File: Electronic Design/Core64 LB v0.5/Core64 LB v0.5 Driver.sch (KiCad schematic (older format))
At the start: 68 parts, among them J11 SSW-116-22-F-S-VS‎, J13 Core Cur. Mon., J14 SSW-116-22-F-S-VS‎, Q10 MMBT4403LT1G, Q11 MMBT4403LT1G, Q12 MMBT4401LT1G, Q13 MMBT4403LT1G, Q14 MMBT4403LT1G, Q15 MMBT4401LT1G, Q16 MMBT4403LT1G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

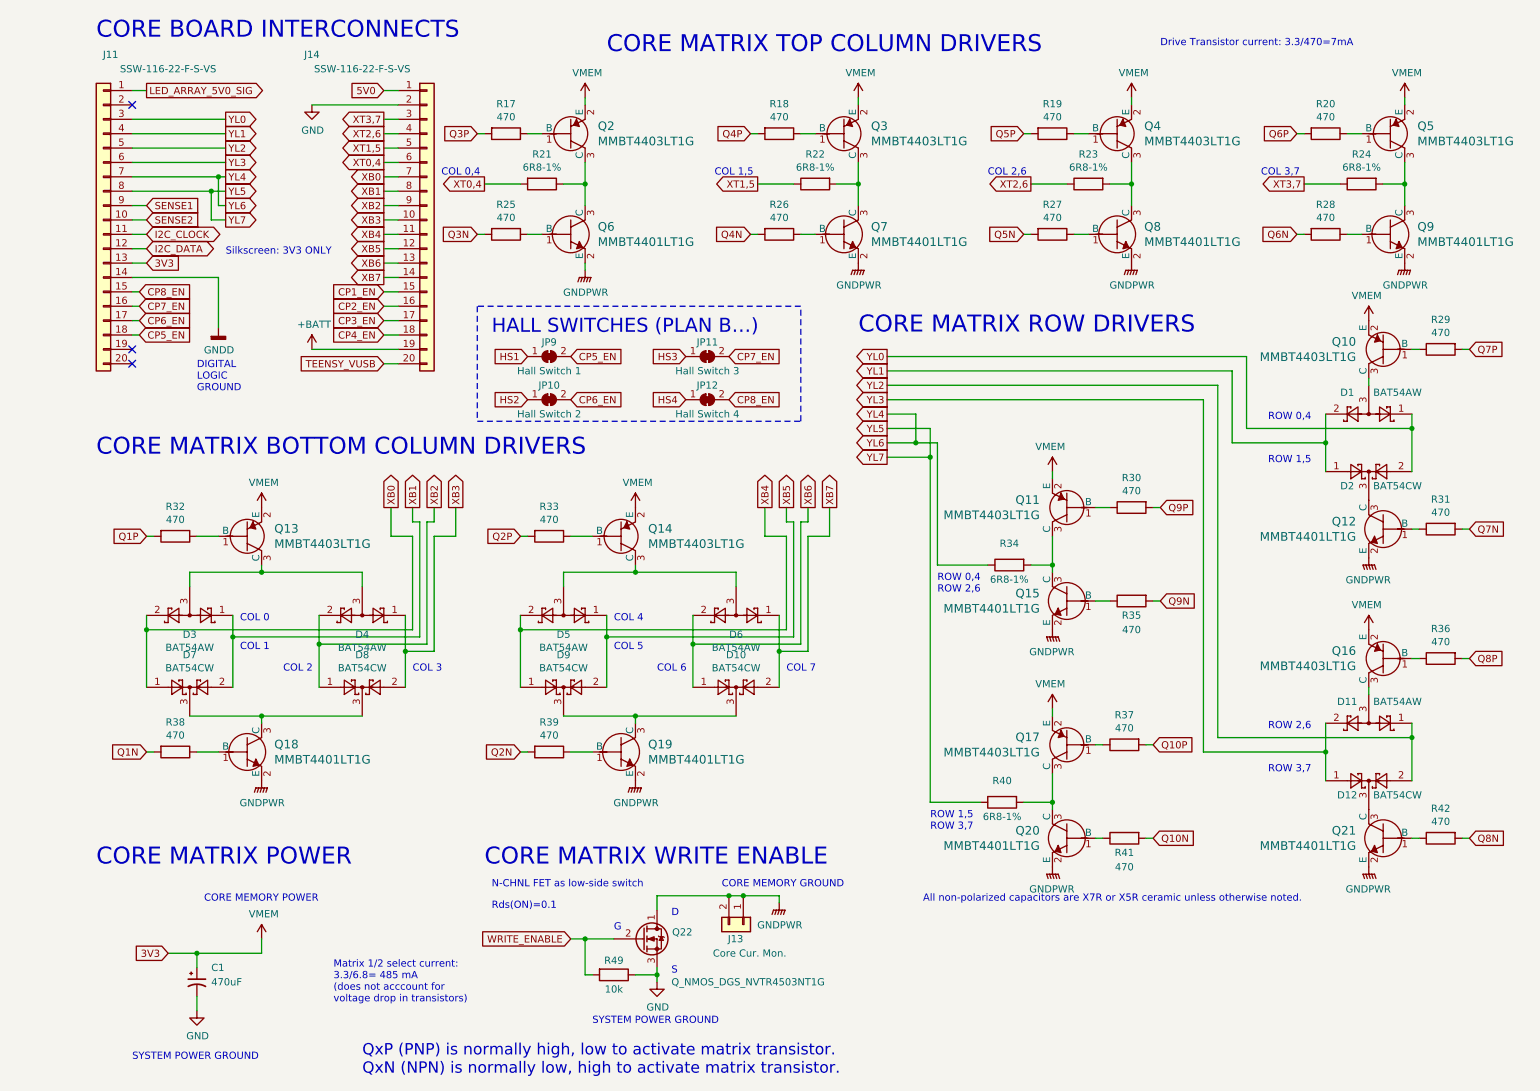
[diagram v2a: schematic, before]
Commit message: Connect row-col-0 to analog inputs for self-test mode
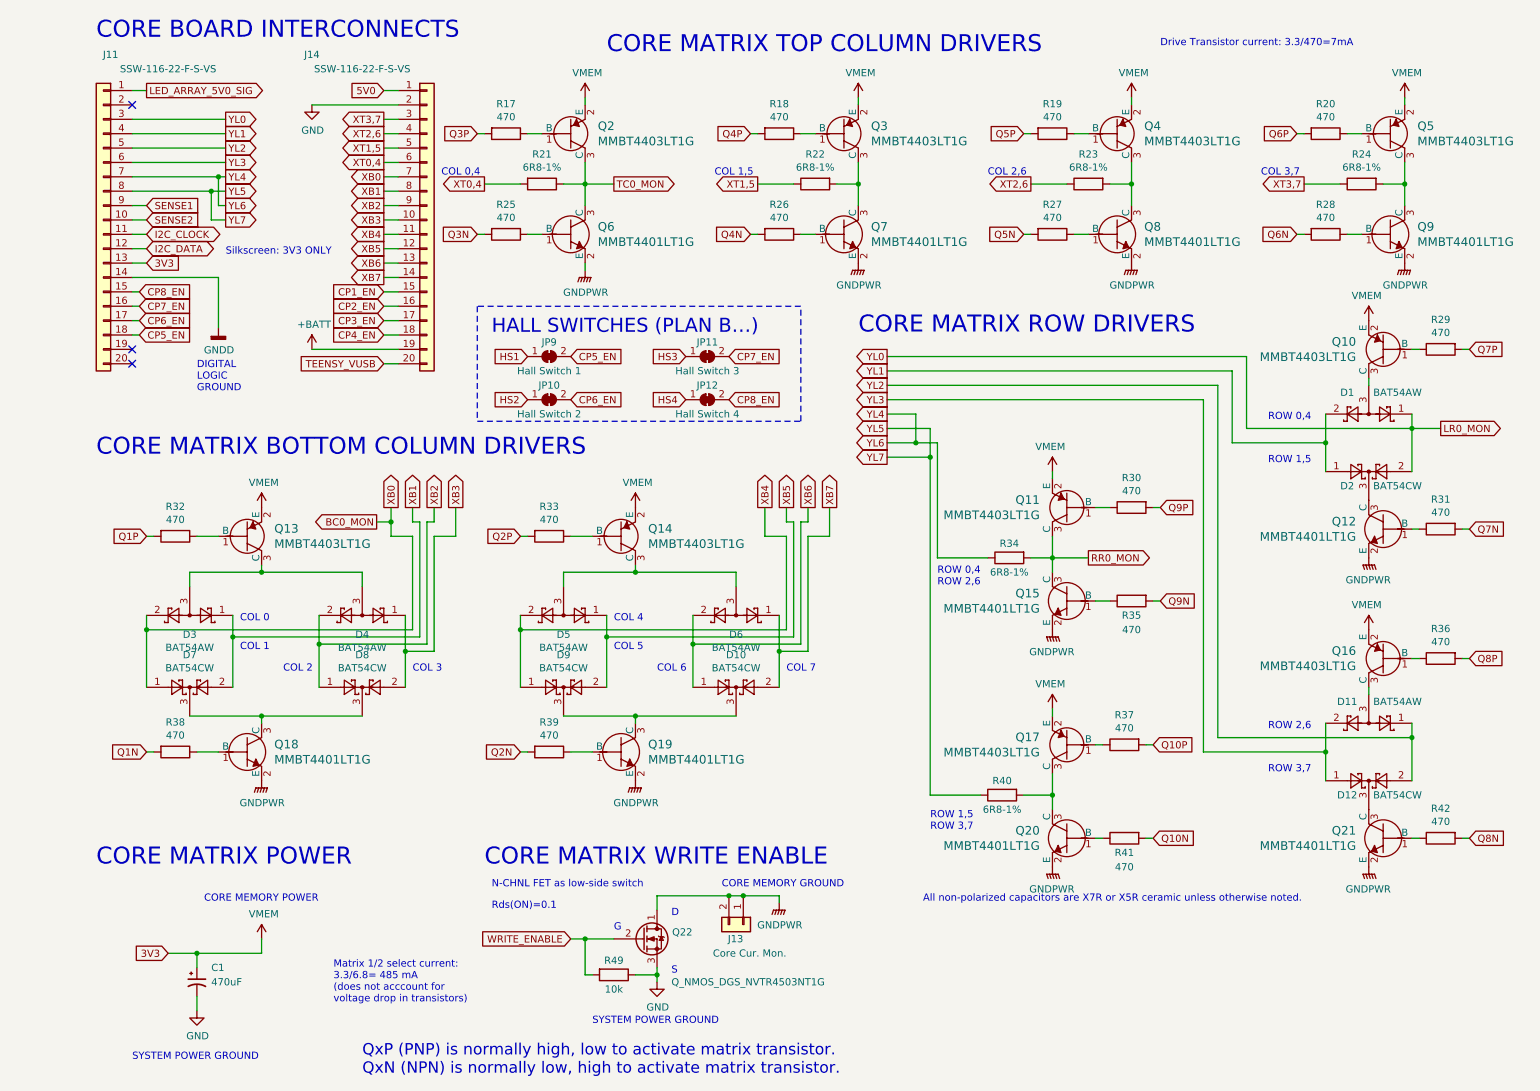
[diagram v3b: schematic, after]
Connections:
- net TC0_MON: now reaches Q2.3 (C), Q6.3 (C), R21.1
- net RR0_MON: now reaches Q11.3 (C), Q15.3 (C), R34.2
- net XB0 renamed BC0_MON
- net YL0 renamed LR0_MON
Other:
- moved on the sheet: R34, R40
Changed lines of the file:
@@
 Wire Wire Line
 	2750 4850 2750 4200
-Wire Wire Line
-	900  4850 900  5250
 Connection ~ 900  4850
 Wire Wire Line
@@
 L Device:R R34
 U 1 1 5D6B8249
-P 6900 4400
-F 0 "R34" V 6750 4400 50  0000 C CNN
-F 1 "6R8-1%" V 7000 4400 50  0000 C CNN
-F 2 "Resistor_SMD:R_0805_2012Metric" V 6830 4400 50  0001 C CNN
-F 3 "~" H 6900 4400 50  0001 C CNN
-	1    6900 4400
+P 6900 4350
+F 0 "R34" V 6800 4350 50  0000 C CNN
+F 1 "6R8-1%" V 7000 4350 50  0000 C CNN
+F 2 "Resistor_SMD:R_0805_2012Metric" V 6830 4350 50  0001 C CNN
+F 3 "~" H 6900 4350 50  0001 C CNN
+	1    6900 4350
 	0    -1   1    0
 $EndComp
@@
 $EndComp
 Wire Wire Line
-	7050 4400 7200 4400
-Wire Wire Line
-	7200 4400 7200 4450
-Wire Wire Line
-	7200 4200 7200 4400
-Connection ~ 7200 4400
-Wire Wire Line
 	6050 3350 6250 3350
 Wire Wire Line
@@
 L Device:R R40
 U 1 1 5D87AEBB
-P 6850 6050
-F 0 "R40" V 6700 6050 50  0000 C CNN
-F 1 "6R8-1%" V 6950 6050 50  0000 C CNN
-F 2 "Resistor_SMD:R_0805_2012Metric" V 6780 6050 50  0001 C CNN
-F 3 "~" H 6850 6050 50  0001 C CNN
-	1    6850 6050
+P 6850 6000
+F 0 "R40" V 6750 6000 50  0000 C CNN
+F 1 "6R8-1%" V 6950 6000 50  0000 C CNN
+F 2 "Resistor_SMD:R_0805_2012Metric" V 6780 6000 50  0001 C CNN
+F 3 "~" H 6850 6000 50  0001 C CNN
+	1    6850 6000
 	0    -1   1    0
 $EndComp
@@
 $EndComp
 Wire Wire Line
-	7000 6050 7200 6050
-Wire Wire Line
-	7200 6050 7200 6100
-Wire Wire Line
-	7200 5850 7200 6050
-Connection ~ 7200 6050
-Wire Wire Line
-	6350 3650 6350 6050
+	7000 6000 7200 6000
+Wire Wire Line
+	7200 6000 7200 6100
+Wire Wire Line
+	7200 5850 7200 6000
+Connection ~ 7200 6000
+Wire Wire Line
+	6350 3650 6350 6000
 Wire Wire Line
 	6350 3650 6050 3650
@@
 Text Notes 5350 5150 0    50   ~ 0
 COL 7
-Text Notes 6400 4600 0    50   ~ 0
+Text Notes 6400 4550 0    50   ~ 0
 ROW 0,4\nROW 2,6
 Text Notes 6350 6250 0    50   ~ 0
@@
 	4450 7250 4450 7300
 Wire Wire Line
-	2600 4000 2600 4200
+	2600 4000 2600 4100
 Wire Wire Line
 	2600 4200 2750 4200
@@
 Connection ~ 6350 3650
 Wire Wire Line
-	6400 3550 6400 4400
+	6400 3550 6400 4350
 Wire Wire Line
 	6250 3550 6400 3550
@@
 $EndComp
 Wire Wire Line
-	3250 1750 3500 1750
-Wire Wire Line
 	1250 7200 1250 7100
 Connection ~ 1250 7100
@@
 $EndComp
 Wire Wire Line
-	6400 4400 6750 4400
-Wire Wire Line
-	6350 6050 6700 6050
+	6400 4350 6750 4350
+Wire Wire Line
+	6350 6000 6700 6000
 Wire Wire Line
 	5050 6700 5300 6700
@@
 Text Notes 3300 2800 0    98   ~ 0
 HALL SWITCHES (PLAN B…)
+Text GLabel 4150 1750 2    50   Output ~ 0
+TC0_MON
+Text GLabel 2500 4100 0    50   Output ~ 0
+BC0_MON
+Wire Wire Line
+	900  4850 900  5250
+Text GLabel 7450 4350 2    50   Output ~ 0
+RR0_MON
+Text GLabel 9900 3450 2    50   Output ~ 0
+LR0_MON
+Wire Wire Line
+	2500 4100 2600 4100
+Connection ~ 2600 4100
+Wire Wire Line
+	2600 4100 2600 4200
+Wire Wire Line
+	3250 1750 3500 1750
+Wire Wire Line
+	3950 1750 4150 1750
+Wire Wire Line
+	9700 3450 9900 3450
+Wire Wire Line
+	7200 4200 7200 4350
+Wire Wire Line
+	7200 4350 7200 4450
+Connection ~ 7200 4350
+Wire Wire Line
+	7050 4350 7200 4350
+Wire Wire Line
+	7200 4350 7450 4350
 $EndSCHEMATC

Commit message: Update schematic battery and LiPo charger notes, move SD_CD from ANA_6 to SPARE_3, schematic red lines
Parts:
- Q22: symbol Device:Q_NMOS_DGS -> Device:Q_NMOS_GSD
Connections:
- net GND: now also Q22.2 (S); no longer Q22.3 (S)
- net GNDPWR: now also Q22.3 (D); no longer Q22.1 (D)
- net WRITE_ENABLE: now also Q22.1 (G); no longer Q22.2 (G)
- net LED_ARRAY_5V0_SIG renamed LED_MATRIX_5V0_SIG
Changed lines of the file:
@@
 Date "2021-02-04"
 Rev "0.5"
-Comp "www.Core64.io"
-Comment1 "Work in progress"
-Comment2 "Andy Geppert"
+Comp "Concept and design by Andy Geppert @ www.MachineIdeas.com"
+Comment1 "Visit www.Core64.io for information on assembly and optional features."
+Comment2 "*** Work in progress ***"
 Comment3 ""
-Comment4 ""
+Comment4 "All non-polarized capacitors are X7R or X5R ceramic unless otherwise noted."
 $EndDescr
 Wire Wire Line
@@
 N-CHNL FET as low-side switch
 $Comp
-L Device:Q_NMOS_DGS Q22
+L Device:Q_NMOS_GSD Q22
 U 1 1 5FABD474
 P 4350 7000
@@
 	2550 1100 2650 1100
 Text GLabel 900  1100 2    50   Output ~ 0
-LED_ARRAY_5V0_SIG
+LED_MATRIX_5V0_SIG
 Wire Wire Line
 	800  1100 900  1100

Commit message: Refine and release LB and CB V0.5 layout for prototyping
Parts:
- J11, J14: footprint Connector_PinHeader_2.54mm:PinHeader_1x20_P2.54mm_Vertical -> Connector_PinSocket_2.54mm:PinSocket_1x20_P2.54mm_Vertical
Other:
- note removed: "All non-polarized capacitors are X7R or X5R ceramic unless otherwise noted."
- note removed: "Matrix 1/2 select current: \n3.3/6.8= 485 mA\n(does not acccount for \nvoltage drop in transistors)"
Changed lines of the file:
@@
 Sheet 5 5
 Title "Core 64 - Core Matrix Driver"
-Date "2021-02-04"
+Date "2021-02-27"
 Rev "0.5"
 Comp "Concept and design by Andy Geppert @ www.MachineIdeas.com"
 Comment1 "Visit www.Core64.io for information on assembly and optional features."
-Comment2 "*** Work in progress ***"
+Comment2 "*** As prototyped. ***"
 Comment3 ""
 Comment4 "All non-polarized capacitors are X7R or X5R ceramic unless otherwise noted."
@@
 	1    0    0    -1
 $EndComp
-Text Notes 2200 7450 0    50   ~ 0
-Matrix 1/2 select current: \n3.3/6.8= 485 mA\n(does not acccount for \nvoltage drop in transistors)
 Text Notes 2950 1700 0    50   ~ 0
 COL 0,4
@@
 F 0 "J14" H 2050 3150 50  0000 C CNN
 F 1 "SSW-116-22-F-S-VS‎" H 2400 3050 50  0000 C CNN
-F 2 "Connector_PinHeader_2.54mm:PinHeader_1x20_P2.54mm_Vertical" H 2850 2000 50  0001 C CNN
+F 2 "Connector_PinSocket_2.54mm:PinSocket_1x20_P2.54mm_Vertical" H 2850 2000 50  0001 C CNN
 F 3 "~" H 2850 2000 50  0001 C CNN
 	1    2850 2000
@@
 F 0 "J11" H 550 3150 50  0000 C CNN
 F 1 "SSW-116-22-F-S-VS‎" H 150 3050 50  0000 C CNN
-F 2 "Connector_PinHeader_2.54mm:PinHeader_1x20_P2.54mm_Vertical" H 600 2000 50  0001 C CNN
+F 2 "Connector_PinSocket_2.54mm:PinSocket_1x20_P2.54mm_Vertical" H 600 2000 50  0001 C CNN
 F 3 "~" H 600 2000 50  0001 C CNN
 	1    600  2000
@@
 	1    0    0    -1
 $EndComp
-Text Notes 6300 6750 0    50   ~ 0
-All non-polarized capacitors are X7R or X5R ceramic unless otherwise noted.
 Text Notes 1450 2250 0    50   ~ 0
 Silkscreen: 3V3 ONLY
